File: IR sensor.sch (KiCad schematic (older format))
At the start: 21 parts, among them P1 BNC, P2 BNC, P3 BNC, P4 CONN_01X02, Q1 SOT-23-3 NPN, U1 TLV2770IDGKR, U2 LM311MX/NOPB

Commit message: ENH: Updates to IR sensors
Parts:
- removed D1: LED, Pin_Headers:Pin_Header_Straight_1x02, symbol LED
- removed P1, P2, P3: BNC, Pin_Headers:Pin_Header_Straight_1x02, symbol BNC
- removed P4: CONN_01X02, Pin_Headers:Pin_Header_Straight_1x02, symbol CONN_01X02
- removed RV1: POT, Pin_Headers:Pin_Header_Straight_1x03, symbol POT
- added P1: CONN_01X08, Terminal_Blocks:TerminalBlock_Pheonix_MPT-2.54mm_8pol, symbol CONN_01X08
- added P2: CONN_01X07, Terminal_Blocks:TerminalBlock_Pheonix_MPT-2.54mm_7pol, symbol CONN_01X07
- U1: value TLV2770IDGKR -> TLV2770
- U2: value LM311MX/NOPB -> LM311
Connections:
- net +5V: now also P2.5 (P5), P2.6 (P6)
- net GND: now also P1.1 (P1), P1.3 (P3), P1.5 (P5), P1.7 (P7), P2.1 (P1), P2.3 (P3), P2.7 (P7)
- net S+: now reaches R2.2, R3.2
- net S+: now also P1.6 (P6)
- net E+: now reaches R1.2
- net E+: now also P1.4 (P4)
- net IR+: now reaches C3.1, U1.2 (-), U1.6, U2.2 (+)
- net IR+: now also P1.8 (P8)
- net POT2: now reaches U2.3 (-)
- net POT2: now also P2.4 (P4)
- net TTL+: now reaches R5.2, R6.2, U2.7
- net TTL+: now also P1.2 (P2)
- net LED+: now reaches Q1.3 (E)
- net LED+: now also P2.2 (P2)
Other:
- note added: "* R4+C2 form a lowpass circuit with fc = 1/(2piRC). \n Selected values give us a cutoff of 160 Hz.\n* C3 helps stabilize the response of the op-amp.\n* C4 and C5 are power supply bypass.\n\nResistors\n* R1 selected to provide a current of less than 50mA to IR LED."
- moved on the sheet: C5, Q1, R1, R5, R6, R7, U2

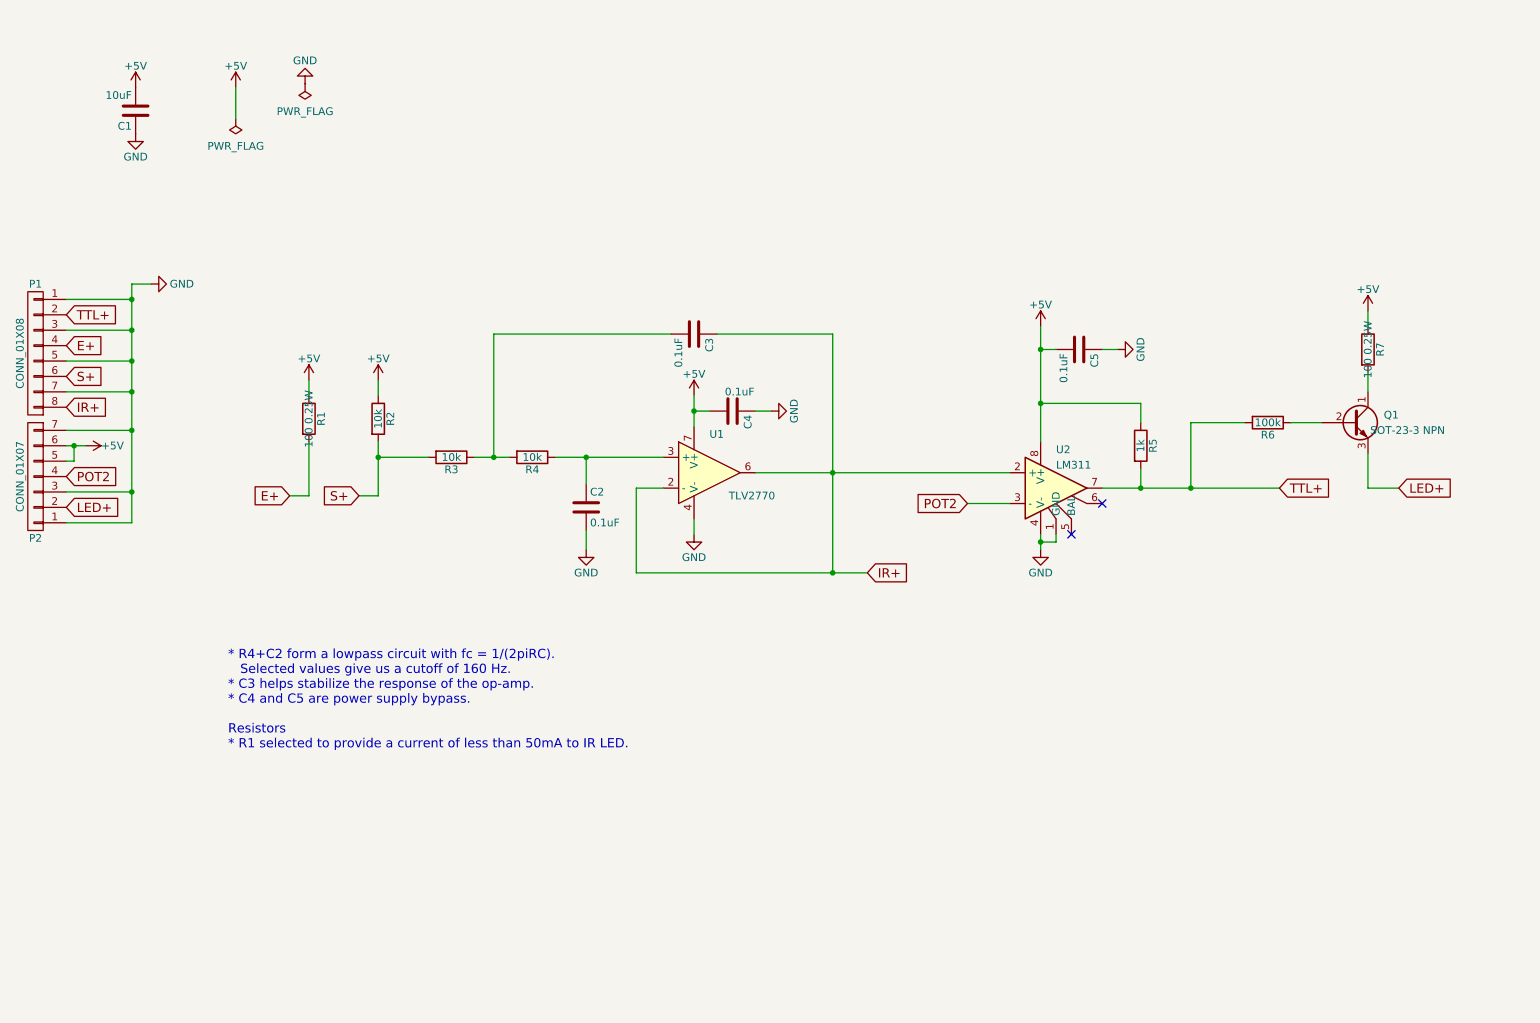
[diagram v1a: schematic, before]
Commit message: ENH: Make PCB more compact
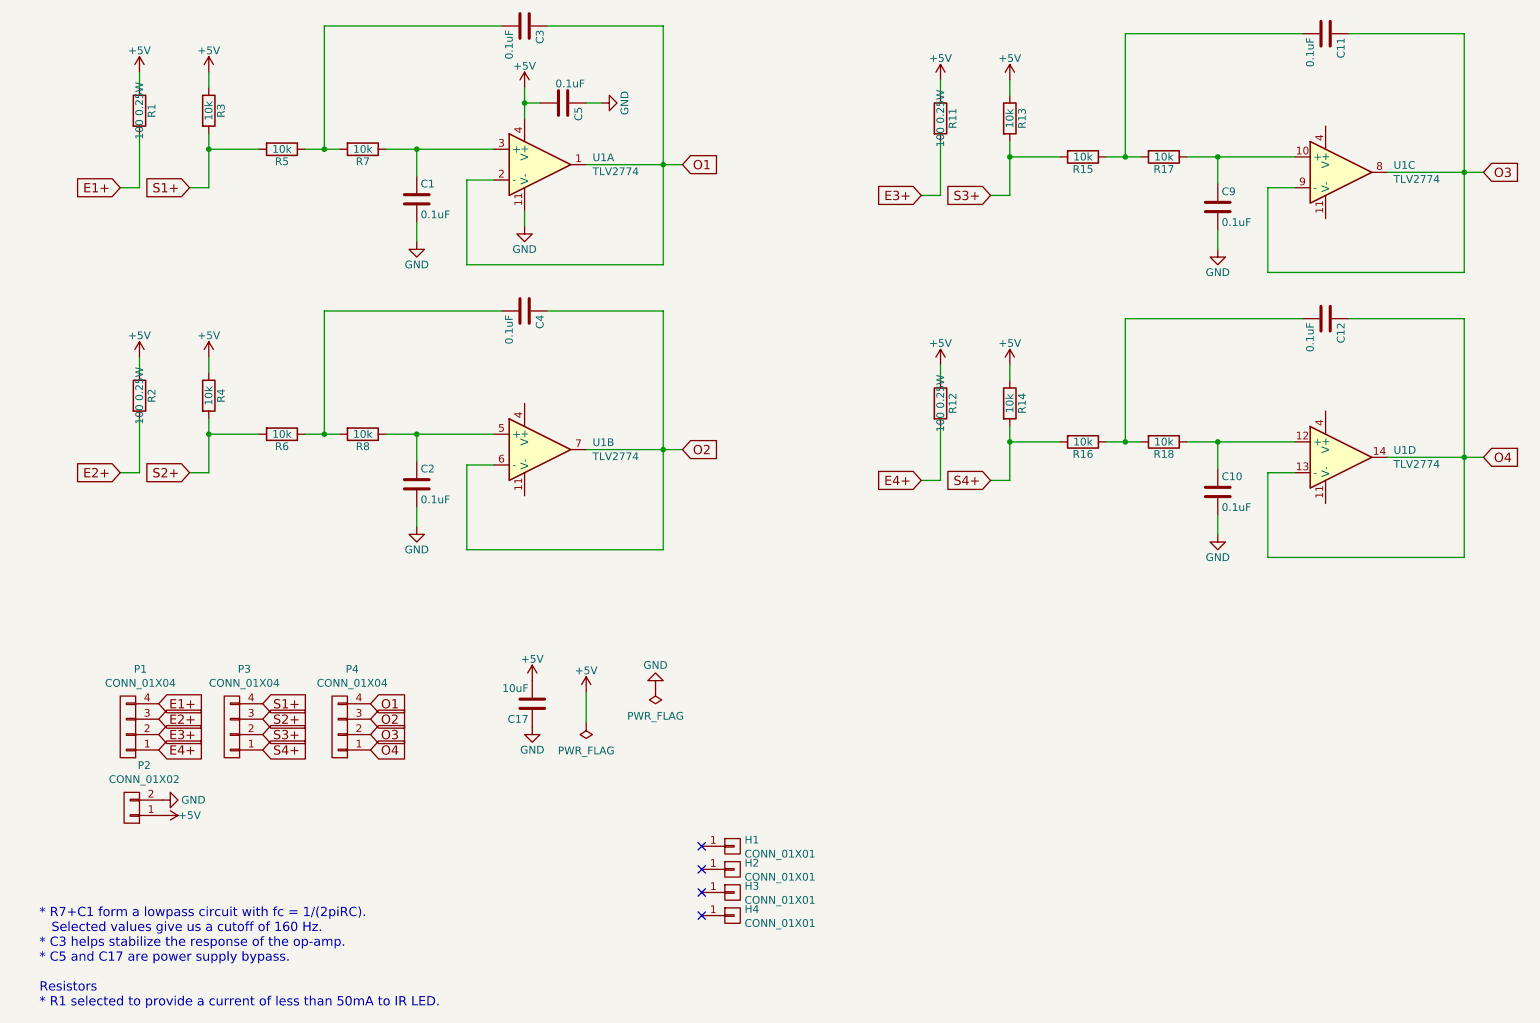
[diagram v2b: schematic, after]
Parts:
- removed C5: 0.1uF, Capacitors_SMD:C_0603, symbol C
- removed P1: CONN_01X08, Terminal_Blocks:TerminalBlock_Pheonix_MPT-2.54mm_8pol, symbol CONN_01X08
- removed P2: CONN_01X07, Terminal_Blocks:TerminalBlock_Pheonix_MPT-2.54mm_7pol, symbol CONN_01X07
- removed Q1: SOT-23-3 NPN, TO_SOT_Packages_SMD:SOT-23, symbol Q_NPN_CBE
- removed R5: 1k, Resistors_SMD:R_0402, symbol R
- removed R7: 100 0.25W, Resistors_SMD:R_1206, symbol R
- removed U1: TLV2770, SMD_Packages:SOIC-8-N, symbol TL071
- removed U2: LM311, SMD_Packages:SOIC-8-N, symbol LM311N
- added C10, C11, C12, C2, C4, C9: 0.1uF, Capacitors_SMD:C_0603, symbol C
- added H1, H2, H3, H4: CONN_01X01, Connect:1pin, symbol CONN_01X01
- added P1, P3, P4: CONN_01X04, Pin_Headers:Pin_Header_Straight_1x04, symbol CONN_01X04
- added P2: CONN_01X02, Pin_Headers:Pin_Header_Straight_1x02, symbol CONN_01X02
- added R11, R12, R2: 100 0.25W, Resistors_SMD:R_1206, symbol R
- added R13, R14, R15, R16, R17, R18, R4, R8: 10k, Resistors_SMD:R_0402, symbol R
- added U1: TLV2774, Housings_SSOP:TSSOP-14_4.4x5mm_Pitch0.65mm, symbol LM2902N
- R6: value 100k -> 10k
- renumbered C2 to C1, C1 to C17, C4 to C5, R2 to R3, R3 to R5, R4 to R7
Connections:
- net +5V: now also P2.1 (P1), R11.1, R12.1, R13.1, R14.1, R2.1, R4.1, U1.4 (V+)
- net GND: now also C10.2, C2.2, C9.2, P2.2 (P2), U1.11 (V-)
- net at C1.1, R7.1: now also U1.3 (+)
- net at R6.1: now also C4.2, R8.2
- net E+ renamed E1+
- net E1+: now also P1.4 (P4)
- net IR+ renamed O1
- net O1: now also P4.4 (P4), U1.1, U1.2 (-)
- net S+ renamed S1+
- net S1+: now also P3.4 (P4)
- net TTL+ renamed S2+
- net S2+: now also P3.3 (P3), R4.2
- new net: C2.1, R8.1, U1.5 (+)
- new net: C11.2, R15.1, R17.2
- new net: C9.1, R17.1, U1.10 (+)
- new net: C12.2, R16.1, R18.2
- new net: C10.1, R18.1, U1.12 (+)
- new net E2+: P1.3 (P3), R2.2
- new net E3+: P1.2 (P2), R11.2
- new net E4+: P1.1 (P1), R12.2
- new net O2: C4.1, P4.3 (P3), U1.6 (-), U1.7
- new net O3: C11.1, P4.2 (P2), U1.8, U1.9 (-)
- new net O4: C12.1, P4.1 (P1), U1.13 (-), U1.14
- new net S3+: P3.2 (P2), R13.2, R15.2
- new net S4+: P3.1 (P1), R14.2, R16.2
- no-connect marks 2 -> 4
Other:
- note added: "* R7+C1 form a lowpass circuit with fc = 1/(2piRC). \n Selected values give us a cutoff of 160 Hz.\n* C3 helps stabilize the response of the op-amp.\n* C5 and C17 are power supply bypass.\n\nResistors\n* R1 selected to provide a current of less than 50mA to IR LED."
- note removed: "* R4+C2 form a lowpass circuit with fc = 1/(2piRC). \n Selected values give us a cutoff of 160 Hz.\n* C3 helps stabilize the response of the op-amp.\n* C4 and C5 are power supply bypass.\n\nResistors\n* R1 selected to provide a current of less than 50mA to IR LED."
- moved on the sheet: C1, C17, C3, C5, R1, R3, R5, R7
